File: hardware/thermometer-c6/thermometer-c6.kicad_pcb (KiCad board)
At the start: 2 copper layers, 48 x 35 mm, 101 parts, among them J1 JST-PH-2 BAT, J2 MEAS_HDR, J3 USB-C, J4 EPD FPC24 0.5mm, J5 DEBUG, Q1 AO3401A, Q2 AO3401A, Q3 Si1308EDL, Q4 AO3401A, Q5 2N7002, Q6 AO3401A, SW1 RESET, SW2 BOOT, U1 ESP32-C6-MINI-1-N4, U2 RT9080-33GJ5, U3 USBLC6-2SC6, U4 MCP73831-2, U5 BMP581, U6 BMP585, Y1 32.768kHz FC-135

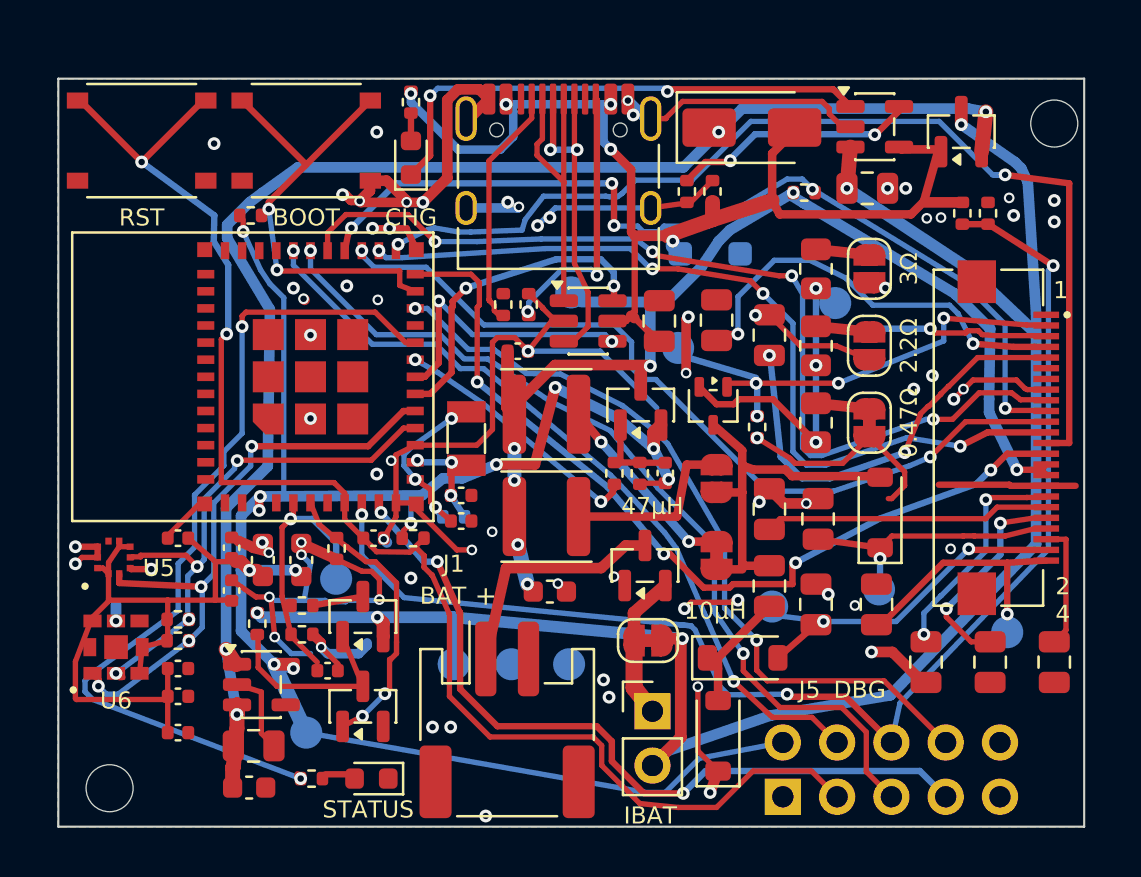
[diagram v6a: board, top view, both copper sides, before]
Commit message: Harvest H1-clearance reroute (VBAT/EPD_SCK) + NE GND re-stitch
User rerouted VBAT + EPD_SCK away from mounting hole H1: nearest non-pour copper 2.32mm -> 3.05mm, so a full 5mm M2 washer now clears. NE GND re-stitched (STITCH: +0.5/0.3 @43.5,5.8, +0.6/0.3 @46.5,6.6 & @46.5,7.6, dropped 46.6,6.7). GND fully connected (0 unconnected), make check green, REAL=0. DEFERRED: 2 via_dangling on redundant vias (44.49,5.58 / 46.6,5.7) — one-sided in the generated zone-fill (non-byte-stable), neither is sole-tie for any pad, so benign.

Co-Authored-By: Claude Opus 4.8 (1M context) <noreply@anthropic.com>
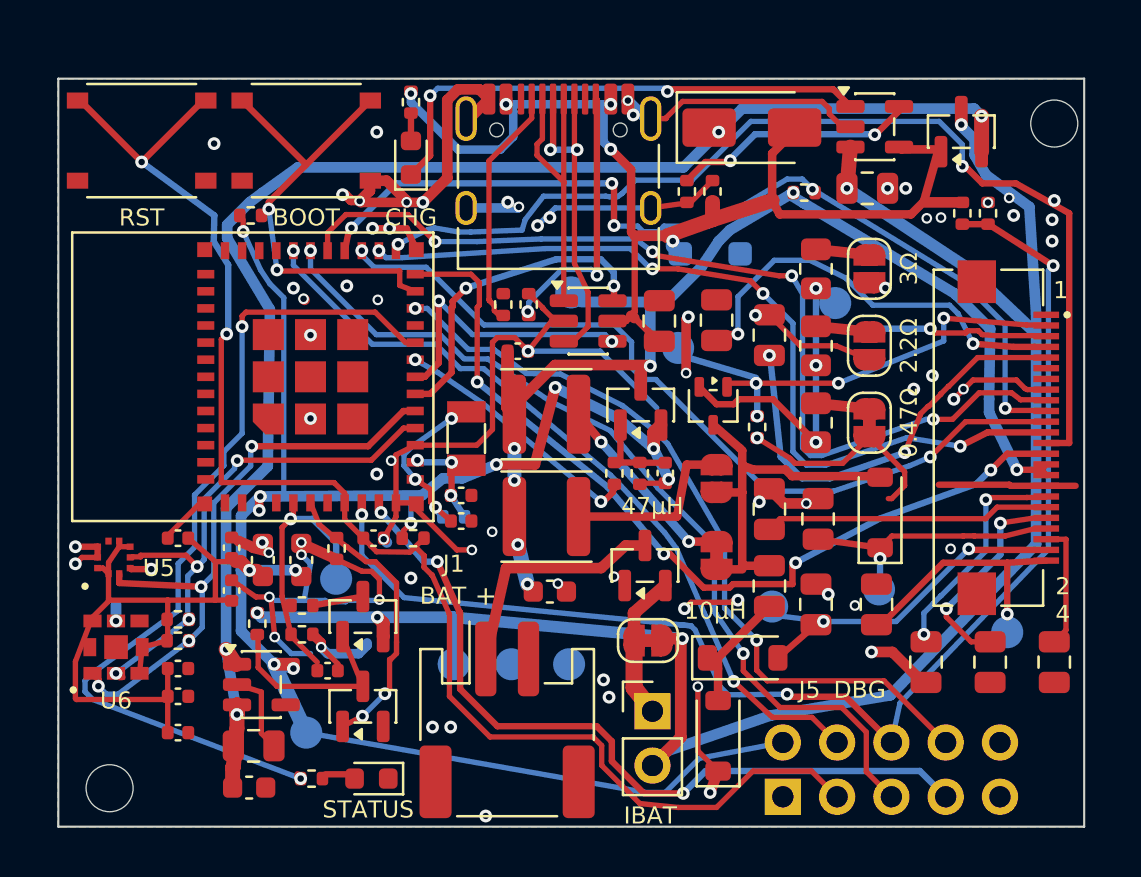
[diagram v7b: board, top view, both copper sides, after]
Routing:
- net EPD_SCK: track 48.7 -> 47.9 mm, vias 2 -> 3
- net VBAT: track 86.6 -> 86.5 mm, vias 5 -> 6

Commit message: Reposition H1/H2 symmetric (>=1mm edges) + harvest Q1/R22/R23 move clearing H1 courtyard
Mounting holes H1->(45.8,2.2)/H2->(2.2,32.8): 180deg-symmetric, >=1mm wall to every board edge (was H1 0.30mm = JLC hole-to-edge DFM fail). H1's screw courtyard then overlapped Q1 at the NE corner; user hand-moved Q1->(41.6,5.04), R22->(41.2,7.6 rot0), R23->(44.0,7.11) and rerouted VSYS/VBUS to clear it. Harvested PLACE (5 refs) + pcb_routes (VBAT-4/EPD_SCK-3/VSYS+2/VBUS+1) + GND re-stitch (7 vias removed incl 2 now-redundant that the user deleted -> via_dangling 0, +1 via +1 track). Gate: 0 unconnected, REAL=0, courtyards_overlap=0, make check green, byte-stable, out/hand==generated.

Co-Authored-By: Claude Opus 4.8 (1M context) <noreply@anthropic.com>
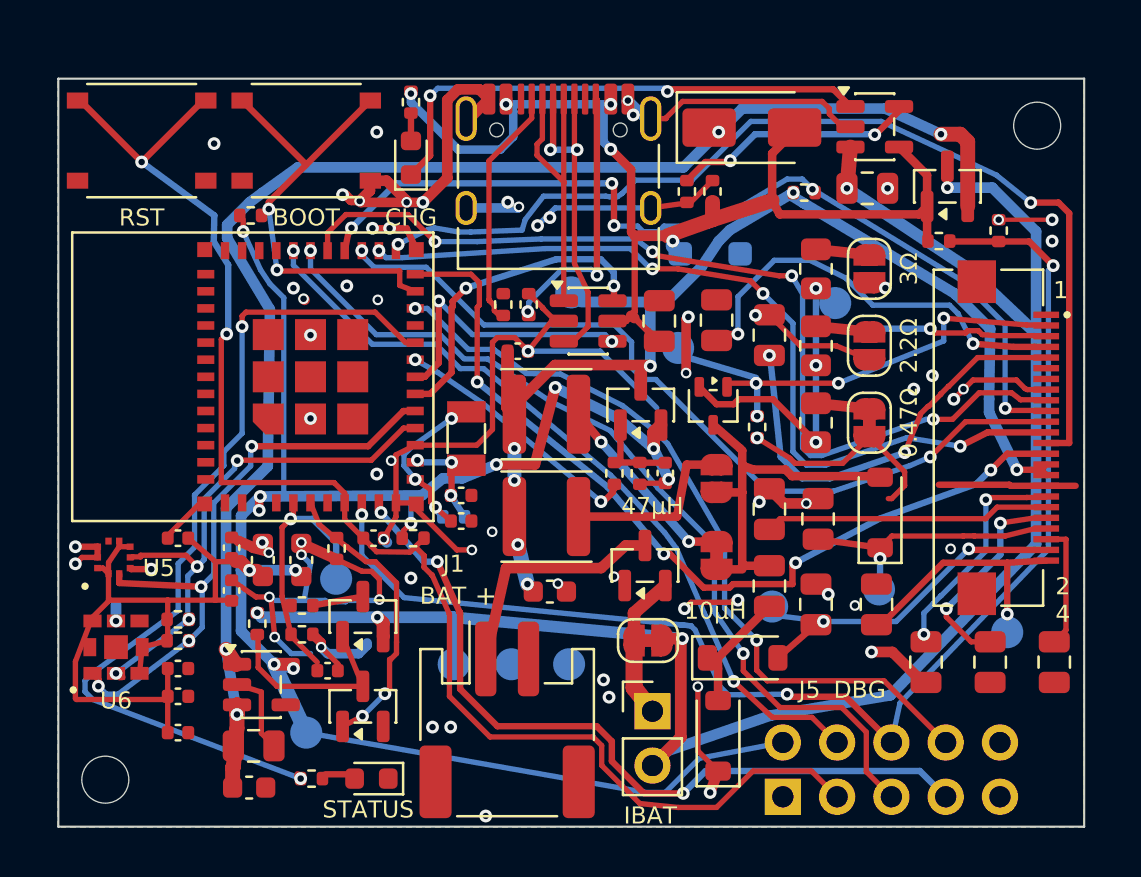
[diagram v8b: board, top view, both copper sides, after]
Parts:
- moved Q1 2.64 mm to (141.6, 105.0)
- moved R22 1.70 mm to (141.2, 107.6), turned to 0 degrees
- moved R23 0.95 mm to (144.0, 107.1)
- moved H1 0.81 mm to (145.8, 102.2)
- moved H2 0.45 mm to (102.2, 132.8)
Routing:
- net GND: track 152.3 -> 154.8 mm, vias 73 -> 69
- net VBAT: track 86.5 -> 85.1 mm, vias 6 -> 5
- net VBUS: track 52.5 -> 51.5 mm
- net VSYS: track 69.4 -> 70.4 mm
- net EPD_SCK: track 47.9 -> 47.0 mm, vias 3 -> 2
- net VBUS_SENSE: track 61.7 -> 62.3 mm
